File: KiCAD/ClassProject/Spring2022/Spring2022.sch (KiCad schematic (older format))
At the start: 4 parts, among them U1 FUB-MINI

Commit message: Nearly finished schematic and routing.
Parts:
- gave numbers to parts that had none: 2
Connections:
- net MISO: now reaches U1.23 (P19-MISO)
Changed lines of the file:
@@
 F0 "LED Bar" 50
 F1 "led-bar.sch" 50
-F2 "LED-SDI" I R 1750 1700 50
-F3 "LED-SCLK" I R 1750 1800 50
-F4 "LED-DCLK" I R 1750 1900 50
-F5 "~LED-OE" I R 1750 2000 50
+F2 "LED-SDI" I R 1750 1800 50
+F3 "LED-SCLK" I R 1750 1900 50
+F4 "LED-DCLK" I R 1750 2000 50
+F5 "~LED-OE" I R 1750 2100 50
+F6 "LED-V+" I R 1750 1700 50
 $EndSheet
 $Comp
@@
 Wire Wire Line
 	9350 3200 9350 3300
-$Comp
-L 74_Jacob:+4.5V #PWR0101
-U 1 1 625DDEA1
-P 9350 2550
-F 0 "#PWR0101" H 9350 2400 50  0001 C CNN
-F 1 "+4.5V" H 9350 2723 50  0000 C CNN
-F 2 "" H 9350 2550 50  0001 C CNN
-F 3 "" H 9350 2550 50  0001 C CNN
-	1    9350 2550
-	1    0    0    -1
-$EndComp
 Wire Wire Line
 	9350 2550 9350 2700
-$Comp
-L 74_Jacob:+4.5V #PWR0104
-U 1 1 625DE893
-P 6900 1250
-F 0 "#PWR0104" H 6900 1100 50  0001 C CNN
-F 1 "+4.5V" H 6900 1423 50  0000 C CNN
-F 2 "" H 6900 1250 50  0001 C CNN
-F 3 "" H 6900 1250 50  0001 C CNN
-	1    6900 1250
-	1    0    0    -1
-$EndComp
 Wire Wire Line
 	6900 1250 6900 1450
@@
 Wire Wire Line
 	7050 3250 6700 3250
-Text GLabel 2000 1700 2    50   Input ~ 0
+Text GLabel 2000 1800 2    50   Input ~ 0
 MOSI
 Wire Wire Line
-	2000 1700 1750 1700
-Text GLabel 2000 1800 2    50   Input ~ 0
+	2000 1800 1750 1800
+Text GLabel 2000 1900 2    50   Input ~ 0
 SCK
 Wire Wire Line
-	2000 1800 1750 1800
+	2000 1900 1750 1900
 Text GLabel 5000 2050 0    50   Input ~ 0
 SCK
 Wire Wire Line
 	5000 2050 5350 2050
-Text GLabel 2000 1900 2    50   Input ~ 0
+Text GLabel 2000 2000 2    50   Input ~ 0
 DISPLAY-CLK
-Text GLabel 2000 2000 2    50   Input ~ 0
+Text GLabel 2000 2100 2    50   Input ~ 0
 ~LED-OE
 Wire Wire Line
-	2000 2000 1750 2000
-Wire Wire Line
-	1750 1900 2000 1900
+	2000 2100 1750 2100
+Wire Wire Line
+	1750 2000 2000 2000
 Text GLabel 4500 3000 0    50   Input ~ 0
 DISPLAY-CLK
@@
 MISSING:\n- I2C Pullup Resistors\n- Hookup I2C to uC\n
 $Sheet
-S 1000 4300 750  650
+S 1000 4300 750  1250
 U 62691FC6
 F0 "Accelerometer" 50
 F1 "accelerometer.sch" 50
+F2 "I2C-SCL" B R 1750 4450 50
+F3 "I2C-SDA" B R 1750 4550 50
+F4 "SPI-CS" I R 1750 4750 50
+F5 "SPI-SDO-MISO" I R 1750 4850 50
+F6 "SPI-SDI-MOSI" I R 1750 4950 50
+F7 "I2C-A0" B R 1750 4650 50
+F8 "INT1" O R 1750 5250 50
+F9 "INT2" O R 1750 5350 50
+F10 "SPI-SCLK" I R 1750 5050 50
 $EndSheet
 Text Notes 1150 3950 1    50   ~ 0
 DONE
 $Comp
-L 1_pontech:PLP-000270 R?
+L 1_pontech:PLP-000270 R17
 U 1 1 626677F4
 P 4250 4750
-F 0 "R?" H 4320 4841 50  0000 L CNN
+F 0 "R17" H 4320 4841 50  0000 L CNN
 F 1 "PLP-000270" H 4320 4750 50  0000 L CNN
 F 2 "a_pontech:R_0603_1608Metric" V 4180 4750 50  0001 C CNN
@@
 $EndComp
 $Comp
-L 1_pontech:PLP-000270 R?
+L 1_pontech:PLP-000270 R18
 U 1 1 62667DF1
 P 5150 4750
-F 0 "R?" H 5220 4841 50  0000 L CNN
+F 0 "R18" H 5220 4841 50  0000 L CNN
 F 1 "PLP-000270" H 5220 4750 50  0000 L CNN
 F 2 "a_pontech:R_0603_1608Metric" V 5080 4750 50  0001 C CNN
@@
 	1    0    0    -1
 $EndComp
-$Comp
-L 74_Jacob:+3.3V #PWR?
-U 1 1 626684CA
-P 4250 4450
-F 0 "#PWR?" H 4250 4300 50  0001 C CNN
-F 1 "+3.3V" H 4250 4623 50  0000 C CNN
-F 2 "" H 4250 4450 50  0001 C CNN
-F 3 "" H 4250 4450 50  0001 C CNN
-	1    4250 4450
-	1    0    0    -1
-$EndComp
-$Comp
-L 74_Jacob:+3.3V #PWR?
-U 1 1 62668DF2
-P 5150 4450
-F 0 "#PWR?" H 5150 4300 50  0001 C CNN
-F 1 "+3.3V" H 5150 4623 50  0000 C CNN
-F 2 "" H 5150 4450 50  0001 C CNN
-F 3 "" H 5150 4450 50  0001 C CNN
-	1    5150 4450
-	1    0    0    -1
-$EndComp
 Wire Wire Line
 	5150 4450 5150 4600
@@
 Wire Wire Line
 	6700 2450 7100 2450
-$Comp
-L 74_Jacob:+3.3V #PWR?
-U 1 1 6266BC1F
+Wire Wire Line
+	5350 1650 4450 1650
+Wire Wire Line
+	4450 1650 4450 1550
+Wire Wire Line
+	7650 1600 7650 1650
+Wire Wire Line
+	7650 1650 6700 1650
+Text GLabel 2000 4450 2    50   Input ~ 0
+I2C-SCK
+Text GLabel 2000 4550 2    50   Input ~ 0
+I2C-SDA
+Wire Wire Line
+	2000 4450 1750 4450
+Wire Wire Line
+	1750 4550 2000 4550
+Text GLabel 7050 3150 2    50   Input ~ 0
+MISO
+Wire Wire Line
+	7050 3150 6700 3150
+Text GLabel 2000 4850 2    50   Input ~ 0
+MISO
+Text GLabel 2000 4950 2    50   Input ~ 0
+MOSI
+Wire Wire Line
+	2000 4950 1750 4950
+Wire Wire Line
+	1750 4850 2000 4850
+Text GLabel 2000 5050 2    50   Input ~ 0
+SCK
+Wire Wire Line
+	2000 5050 1750 5050
+Wire Wire Line
+	1900 1550 1900 1700
+Wire Wire Line
+	1900 1700 1750 1700
+Text Notes 1150 2100 1    50   ~ 0
+DONE
+Text Notes 1150 3050 1    50   ~ 0
+DONE
+Text Notes 1150 5450 1    50   ~ 0
+DONE
+$Comp
+L 74_Jacob:+4.5V #PWR0108
+U 1 1 6274567D
+P 6900 1250
+F 0 "#PWR0108" H 6900 1100 50  0001 C CNN
+F 1 "+4.5V" H 6900 1423 50  0000 C CNN
+F 2 "" H 6900 1250 50  0001 C CNN
+F 3 "" H 6900 1250 50  0001 C CNN
+	1    6900 1250
+	1    0    0    -1
+$EndComp
+$Comp
+L 74_Jacob:+4.5V #PWR0109
+U 1 1 62745CC9
+P 9350 2550
+F 0 "#PWR0109" H 9350 2400 50  0001 C CNN
+F 1 "+4.5V" H 9350 2723 50  0000 C CNN
+F 2 "" H 9350 2550 50  0001 C CNN
+F 3 "" H 9350 2550 50  0001 C CNN
+	1    9350 2550
+	1    0    0    -1
+$EndComp
+$Comp
+L 74_Jacob:+4.5V #PWR0110
+U 1 1 62746536
+P 1900 1550
+F 0 "#PWR0110" H 1900 1400 50  0001 C CNN
+F 1 "+4.5V" H 1900 1723 50  0000 C CNN
+F 2 "" H 1900 1550 50  0001 C CNN
+F 3 "" H 1900 1550 50  0001 C CNN
+	1    1900 1550
+	1    0    0    -1
+$EndComp
+$Comp
+L 74_Jacob:+3.3V #PWR0101
+U 1 1 62747748
 P 4450 1550
-F 0 "#PWR?" H 4450 1400 50  0001 C CNN
+F 0 "#PWR0101" H 4450 1400 50  0001 C CNN
 F 1 "+3.3V" H 4450 1723 50  0000 C CNN
 F 2 "" H 4450 1550 50  0001 C CNN
@@
 	1    0    0    -1
 $EndComp
-Wire Wire Line
-	5350 1650 4450 1650
-Wire Wire Line
-	4450 1650 4450 1550
-$Comp
-L 74_Jacob:+3.3V #PWR?
-U 1 1 6266CF06
+$Comp
+L 74_Jacob:+3.3V #PWR0102
+U 1 1 62747E3F
 P 7650 1600
-F 0 "#PWR?" H 7650 1450 50  0001 C CNN
+F 0 "#PWR0102" H 7650 1450 50  0001 C CNN
 F 1 "+3.3V" H 7650 1773 50  0000 C CNN
 F 2 "" H 7650 1600 50  0001 C CNN
@@
 	1    0    0    -1
 $EndComp
-Wire Wire Line
-	7650 1600 7650 1650
-Wire Wire Line
-	7650 1650 6700 1650
+$Comp
+L power:+3V3 #PWR0103
+U 1 1 6274E40E
+P 4250 4450
+F 0 "#PWR0103" H 4250 4300 50  0001 C CNN
+F 1 "+3V3" H 4265 4623 50  0000 C CNN
+F 2 "" H 4250 4450 50  0001 C CNN
+F 3 "" H 4250 4450 50  0001 C CNN
+	1    4250 4450
+	1    0    0    -1
+$EndComp
+$Comp
+L power:+3V3 #PWR0104
+U 1 1 6274F3A8
+P 5150 4450
+F 0 "#PWR0104" H 5150 4300 50  0001 C CNN
+F 1 "+3V3" H 5165 4623 50  0000 C CNN
+F 2 "" H 5150 4450 50  0001 C CNN
+F 3 "" H 5150 4450 50  0001 C CNN
+	1    5150 4450
+	1    0    0    -1
+$EndComp
 $EndSCHEMATC

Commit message: Schematic finished
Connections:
- net DISPLAY-CLK: now also U1.25 (P21)
- net ~LED-OE: now also U1.26 (P22)
- net ~INT1-ACC: now reaches U1.10 (P6-A4)
- net TEMPERATURE: now reaches U1.12 (P8-A6)
- net IR-TX: now reaches U1.21 (P17-TX1)
- net IR-RX: now reaches U1.28 (P24)
- net ~INT2-ACC: now reaches U1.8 (P4-A2)
- net ~CS-ACC: now reaches U1.9 (P5-A3-SS)
- no-connect marks 0 -> 1
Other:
- note removed: "MISSING:\n- I2C Pullup Resistors\n- Hookup I2C to uC\n"
- moved on the sheet: BT1, R17, R18, U1

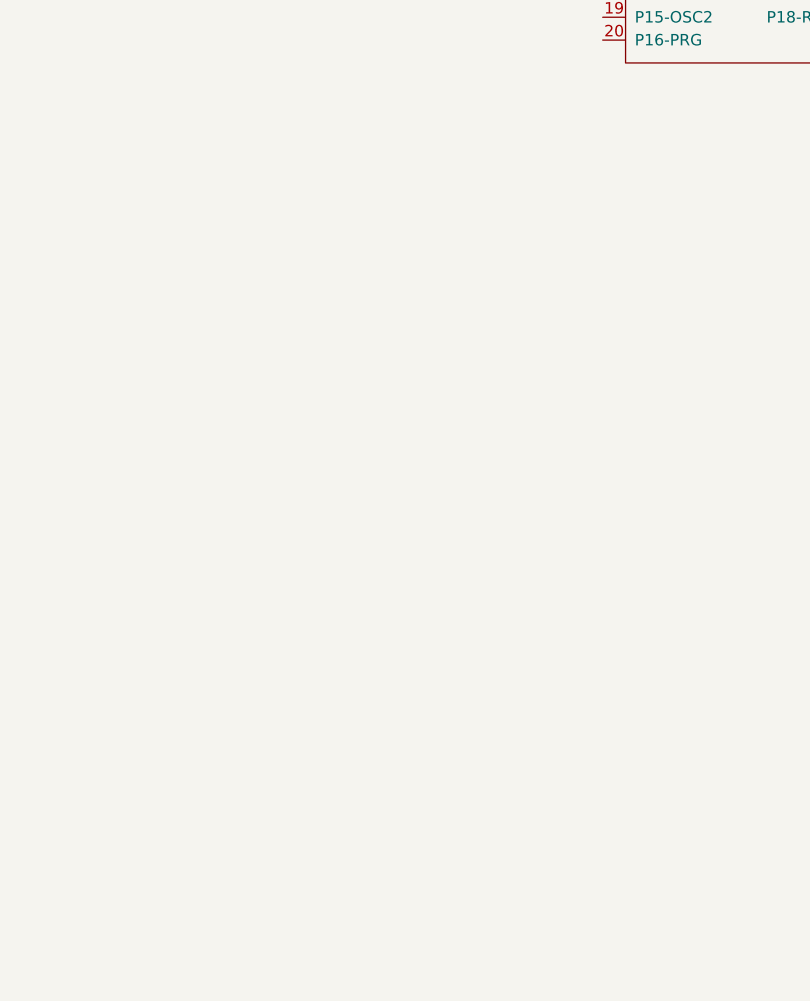
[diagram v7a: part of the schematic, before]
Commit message: Added ESP32 but its going to come off before I am finished.
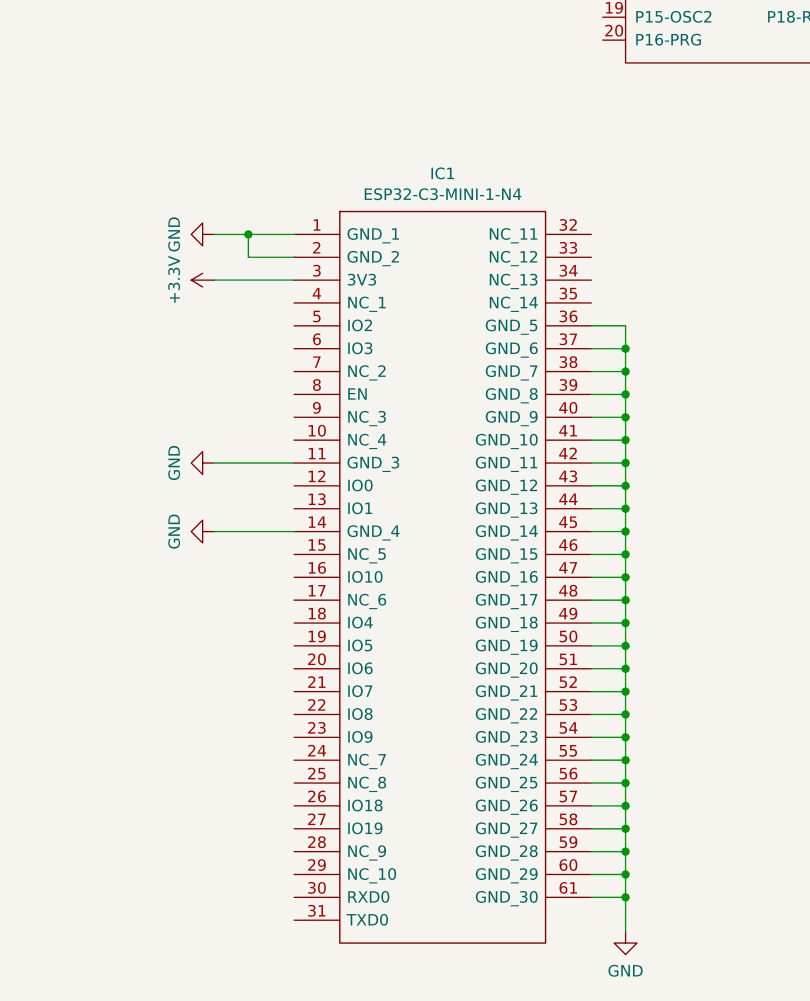
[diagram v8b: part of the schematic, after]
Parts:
- added IC1: ESP32-C3-MINI-1-N4, 74_Patrick B:ESP32C3MINI1N4, symbol 74_Patrick:ESP32-C3-MINI-1-N4
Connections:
- net +3V3: now also IC1.3 (3V3)
- net GND: now also IC1.1 (GND_1), IC1.11 (GND_3), IC1.14 (GND_4), IC1.2 (GND_2), IC1.36 (GND_5), IC1.37 (GND_6), IC1.38 (GND_7), IC1.39 (GND_8), IC1.40 (GND_9), IC1.41 (GND_10), IC1.42 (GND_11), IC1.43 (GND_12), IC1.44 (GND_13), IC1.45 (GND_14), IC1.46 (GND_15), IC1.47 (GND_16), IC1.48 (GND_17), IC1.49 (GND_18), IC1.50 (GND_19), IC1.51 (GND_20), IC1.52 (GND_21), IC1.53 (GND_22), IC1.54 (GND_23), IC1.55 (GND_24), IC1.56 (GND_25), IC1.57 (GND_26), IC1.58 (GND_27), IC1.59 (GND_28), IC1.60 (GND_29), IC1.61 (GND_30)
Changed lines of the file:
@@
 IR-RX
 $Comp
-L 74_Jacob:+3.3V #PWR?
+L 74_Jacob:+3.3V #PWR0103
 U 1 1 6277D0DD
 P 9250 3900
-F 0 "#PWR?" H 9250 3750 50  0001 C CNN
+F 0 "#PWR0103" H 9250 3750 50  0001 C CNN
 F 1 "+3.3V" H 9250 4073 50  0000 C CNN
 F 2 "" H 9250 3900 50  0001 C CNN
@@
 $EndComp
 $Comp
-L 74_Jacob:+3.3V #PWR?
+L 74_Jacob:+3.3V #PWR0104
 U 1 1 6277DF79
 P 10150 3900
-F 0 "#PWR?" H 10150 3750 50  0001 C CNN
+F 0 "#PWR0104" H 10150 3750 50  0001 C CNN
 F 1 "+3.3V" H 10150 4073 50  0000 C CNN
 F 2 "" H 10150 3900 50  0001 C CNN
@@
 Wire Wire Line
 	7100 2450 6700 2450
+$Comp
+L 74_Patrick:ESP32-C3-MINI-1-N4 IC1
+U 1 1 62773C69
+P 4000 4000
+F 0 "IC1" H 4650 4265 50  0000 C CNN
+F 1 "ESP32-C3-MINI-1-N4" H 4650 4174 50  0000 C CNN
+F 2 "74_Patrick B:ESP32C3MINI1N4" H 5150 4100 50  0001 L CNN
+F 3 "https://www.mouser.com/datasheet/2/891/Espressif_ESP32_C3_MINI_1_Datasheet-2006822.pdf" H 5150 4000 50  0001 L CNN
+F 4 "SMD MODULE, ESP32-C3FN4, PCB ANT" H 5150 3900 50  0001 L CNN "Description"
+F 5 "2.55" H 5150 3800 50  0001 L CNN "Height"
+F 6 "Espressif Systems" H 5150 3700 50  0001 L CNN "Manufacturer_Name"
+F 7 "ESP32-C3-MINI-1-N4" H 5150 3600 50  0001 L CNN "Manufacturer_Part_Number"
+F 8 "356-ESP32-C3-MINI1N4" H 5150 3500 50  0001 L CNN "Mouser Part Number"
+F 9 "https://www.mouser.co.uk/ProductDetail/Espressif-Systems/ESP32-C3-MINI-1-N4?qs=stqOd1AaK7%252B%2FpH3qqyGehA%3D%3D" H 5150 3400 50  0001 L CNN "Mouser Price/Stock"
+	1    4000 4000
+	1    0    0    -1
+$EndComp
+Wire Wire Line
+	5300 4400 5450 4400
+Wire Wire Line
+	5450 4400 5450 4500
+Wire Wire Line
+	5450 6900 5300 6900
+$Comp
+L 74_Jacob:GND #PWR?
+U 1 1 62778CA7
+P 5450 7050
+F 0 "#PWR?" H 5450 6800 50  0001 C CNN
+F 1 "GND" H 5450 6877 50  0000 C CNN
+F 2 "" H 5450 7050 50  0001 C CNN
+F 3 "" H 5450 7050 50  0001 C CNN
+	1    5450 7050
+	1    0    0    -1
+$EndComp
+Wire Wire Line
+	5450 7050 5450 6900
+Connection ~ 5450 6900
+Wire Wire Line
+	5300 6800 5450 6800
+Connection ~ 5450 6800
+Wire Wire Line
+	5450 6800 5450 6900
+Wire Wire Line
+	5450 6700 5300 6700
+Connection ~ 5450 6700
+Wire Wire Line
+	5450 6700 5450 6800
+Wire Wire Line
+	5300 6600 5450 6600
+Connection ~ 5450 6600
+Wire Wire Line
+	5450 6600 5450 6700
+Wire Wire Line
+	5450 6500 5300 6500
+Connection ~ 5450 6500
+Wire Wire Line
+	5450 6500 5450 6600
+Wire Wire Line
+	5300 6400 5450 6400
+Connection ~ 5450 6400
+Wire Wire Line
+	5450 6400 5450 6500
+Wire Wire Line
+	5450 6300 5300 6300
+Connection ~ 5450 6300
+Wire Wire Line
+	5450 6300 5450 6400
+Wire Wire Line
+	5300 6200 5450 6200
+Connection ~ 5450 6200
+Wire Wire Line
+	5450 6200 5450 6300
+Wire Wire Line
+	5450 6100 5300 6100
+Connection ~ 5450 6100
+Wire Wire Line
+	5450 6100 5450 6200
+Wire Wire Line
+	5300 6000 5450 6000
+Connection ~ 5450 6000
+Wire Wire Line
+	5450 6000 5450 6100
+Wire Wire Line
+	5450 5900 5300 5900
+Connection ~ 5450 5900
+Wire Wire Line
+	5450 5900 5450 6000
+Wire Wire Line
+	5300 5800 5450 5800
+Connection ~ 5450 5800
+Wire Wire Line
+	5450 5800 5450 5900
+Wire Wire Line
+	5450 5700 5300 5700
+Connection ~ 5450 5700
+Wire Wire Line
+	5450 5700 5450 5800
+Wire Wire Line
+	5300 5600 5450 5600
+Connection ~ 5450 5600
+Wire Wire Line
+	5450 5600 5450 5700
+Wire Wire Line
+	5450 5500 5300 5500
+Connection ~ 5450 5500
+Wire Wire Line
+	5450 5500 5450 5600
+Wire Wire Line
+	5300 5400 5450 5400
+Connection ~ 5450 5400
+Wire Wire Line
+	5450 5400 5450 5500
+Wire Wire Line
+	5450 5300 5300 5300
+Connection ~ 5450 5300
+Wire Wire Line
+	5450 5300 5450 5400
+Wire Wire Line
+	5300 5200 5450 5200
+Connection ~ 5450 5200
+Wire Wire Line
+	5450 5200 5450 5300
+Wire Wire Line
+	5450 5100 5300 5100
+Connection ~ 5450 5100
+Wire Wire Line
+	5450 5100 5450 5200
+Wire Wire Line
+	5300 5000 5450 5000
+Connection ~ 5450 5000
+Wire Wire Line
+	5450 5000 5450 5100
+Wire Wire Line
+	5300 4900 5450 4900
+Connection ~ 5450 4900
+Wire Wire Line
+	5450 4900 5450 5000
+Wire Wire Line
+	5450 4800 5300 4800
+Connection ~ 5450 4800
+Wire Wire Line
+	5450 4800 5450 4900
+Wire Wire Line
+	5300 4700 5450 4700
+Connection ~ 5450 4700
+Wire Wire Line
+	5450 4700 5450 4800
+Wire Wire Line
+	5450 4600 5300 4600
+Connection ~ 5450 4600
+Wire Wire Line
+	5450 4600 5450 4700
+Wire Wire Line
+	5300 4500 5450 4500
+Connection ~ 5450 4500
+Wire Wire Line
+	5450 4500 5450 4600
+Wire Wire Line
+	4000 4100 3800 4100
+Wire Wire Line
+	3800 4100 3800 4000
+Wire Wire Line
+	3800 4000 4000 4000
+$Comp
+L 74_Jacob:GND #PWR?
+U 1 1 627AED84
+P 3650 4000
+F 0 "#PWR?" H 3650 3750 50  0001 C CNN
+F 1 "GND" H 3650 3827 50  0000 C CNN
+F 2 "" H 3650 4000 50  0001 C CNN
+F 3 "" H 3650 4000 50  0001 C CNN
+	1    3650 4000
+	0    1    1    0
+$EndComp
+Wire Wire Line
+	3650 4000 3800 4000
+Connection ~ 3800 4000
+$Comp
+L 74_Jacob:+3.3V #PWR?
+U 1 1 627B2F21
+P 3650 4200
+F 0 "#PWR?" H 3650 4050 50  0001 C CNN
+F 1 "+3.3V" H 3650 4373 50  0000 C CNN
+F 2 "" H 3650 4200 50  0001 C CNN
+F 3 "" H 3650 4200 50  0001 C CNN
+	1    3650 4200
+	0    -1   -1   0
+$EndComp
+Wire Wire Line
+	3650 4200 4000 4200
+$Comp
+L 74_Jacob:GND #PWR?
+U 1 1 627B8310
+P 3650 5000
+F 0 "#PWR?" H 3650 4750 50  0001 C CNN
+F 1 "GND" H 3650 4827 50  0000 C CNN
+F 2 "" H 3650 5000 50  0001 C CNN
+F 3 "" H 3650 5000 50  0001 C CNN
+	1    3650 5000
+	0    1    1    0
+$EndComp
+$Comp
+L 74_Jacob:GND #PWR?
+U 1 1 627B8A2D
+P 3650 5300
+F 0 "#PWR?" H 3650 5050 50  0001 C CNN
+F 1 "GND" H 3650 5127 50  0000 C CNN
+F 2 "" H 3650 5300 50  0001 C CNN
+F 3 "" H 3650 5300 50  0001 C CNN
+	1    3650 5300
+	0    1    1    0
+$EndComp
+Wire Wire Line
+	3650 5300 4000 5300
+Wire Wire Line
+	4000 5000 3650 5000
 $EndSCHEMATC
